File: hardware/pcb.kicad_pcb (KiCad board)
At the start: 2 copper layers, 80 x 30 mm, 4 parts

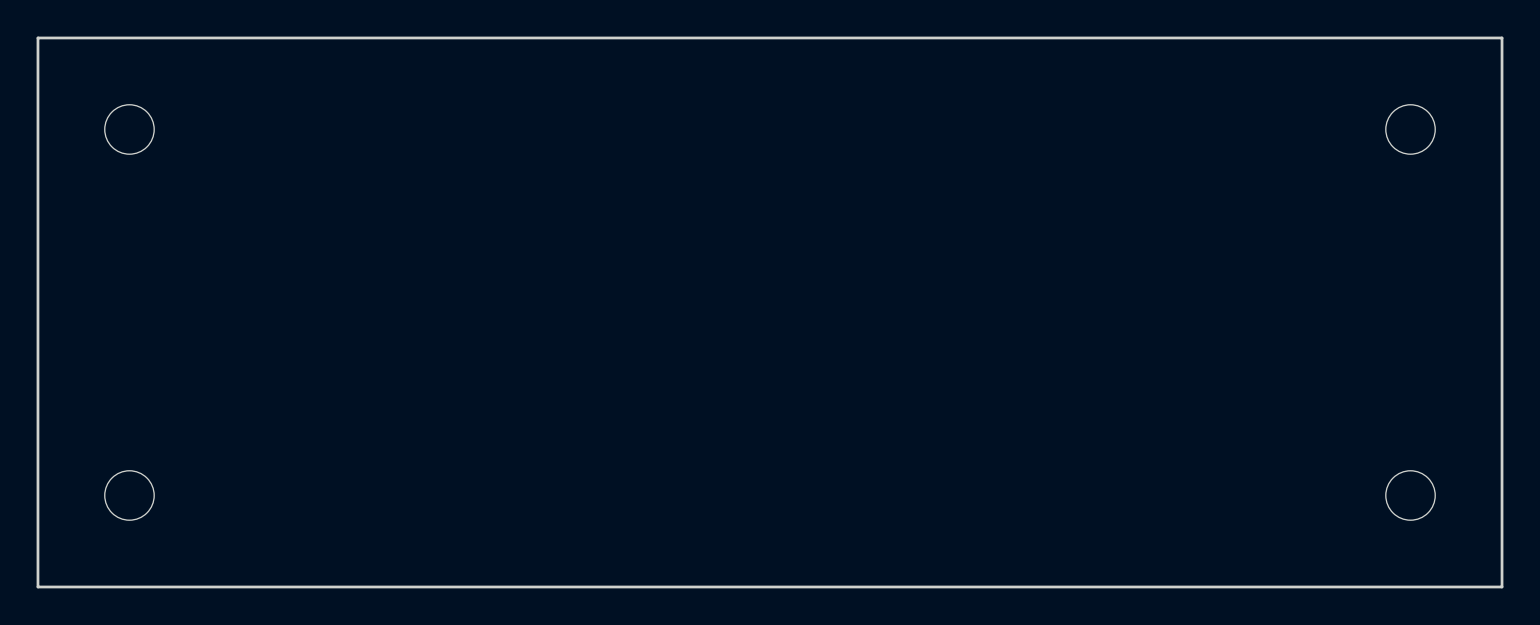
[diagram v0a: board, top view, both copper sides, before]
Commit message: Update PCB layout to show JST connectors on both sides
- Add component placement areas for balanced layout
- 2x JST connectors on left side (J3, J4 for D0, D1)
- 2x JST connectors on right side (J5, J6 for D2, D3)
- ESP32-C3 in center with CAN transceiver
- RJ45 on right, programming header bottom right
- Matches prototype photo layout
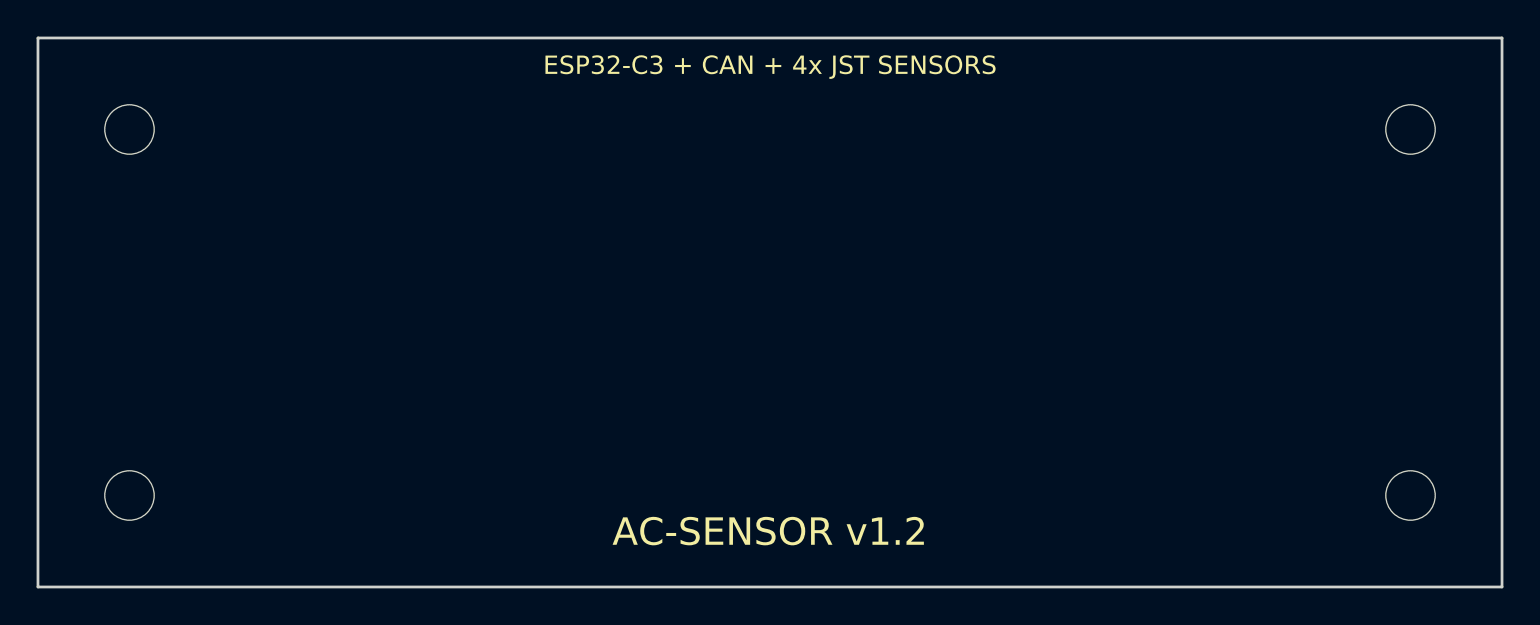
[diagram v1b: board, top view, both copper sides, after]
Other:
- board text added: "AC-SENSOR v1.2"
- board text added: "CAN: GPIO6(TX), GPIO7(RX) RJ45: 1(+5V), 2(GND), 3(H), 4(L)"
- board text added: "ESP32-C3 + CAN + 4x JST SENSORS"
- board text added: "ESP32-C3 CENTER"
- board text added: "J3 SENSOR 1 D0"
- board text added: "J4 SENSOR 2 D1"
- board text added: "J5 SENSOR 3 D2"
- board text added: "J6 SENSOR 4 D3"
- board text added: "JST LAYOUT: LEFT: J3(D0), J4(D1) RIGHT: J5(D2), J6(D3)"
- board text added: "POWER AMS1117-5.0"
- board text added: "PROG 4-PIN"
- board text added: "RJ45 CAN"
- board text added: "RST BOOT"
- board text added: "TJA1050"
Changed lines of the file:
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@@
     (paper "A4")
     (title_block
-      (title "ESP32-C3 CAN Bus + I2C Sensor Board")
+      (title "ESP32-C3 CAN Bus + 4x JST Sensor Board")
       (date "2025-06-02")
-      (rev "v1.0")
+      (rev "v1.2")
       (company "AC-Sensor Project")
-      (comment 1 "80mm x 30mm compact form factor")
+      (comment 1 "80mm x 30mm with JST connectors on both sides")
       (comment 2 "Optimized for JLCPCB automated assembly")
     )
@@
     )
     (pad_to_mask_clearance 0)
-    (pcbplotparams
-      (layerselection 0x00010fc_ffffffff)
-      (plot_on_all_layers_selection 0x0000000_00000000)
-      (disableapertmacros false)
-      (usegerberextensions false)
-      (usegerberattributes true)
-      (usegerberadvancedattributes true)
-      (creategerberjobfile true)
-      (dashed_line_dash_ratio 12.000000)
-      (dashed_line_gap_ratio 3.000000)
-      (svgprecision 4)
-      (plotframeref false)
-      (viasonmask false)
-      (mode 1)
-      (useauxorigin false)
-      (hpglpennumber 1)
-      (hpglpenspeed 20)
-      (hpglpendiameter 15.000000)
-      (dxfpolygonmode true)
-      (dxfimperialunits true)
-      (dxfusepcbnewfont true)
-      (psnegative false)
-      (psa4output false)
-      (plotreference true)
-      (plotvalue true)
-      (plotinvisibletext false)
-      (sketchpadsonfab false)
-      (subtractmaskfromsilk false)
-      (outputformat 1)
-      (mirror false)
-      (drillshape 1)
-      (scaleselection 1)
-      (outputdirectory "")
-    )
   )
   (net 0 "")
-  (net 1 "+3V3")
-  (net 2 "+5V")
-  (net 3 "GND")
-  (net 4 "CAN_TX")
-  (net 5 "CAN_RX")
-  (net 6 "CAN_H")
-  (net 7 "CAN_L")
-  (net 8 "I2C_SDA")
-  (net 9 "I2C_SCL")
-  (net 10 "CAN_SILENT")
-  (net 11 "STATUS_LED")
-  (net 12 "BOOT")
-  (net 13 "RESET")
-  (net 14 "UART_TX")
-  (net 15 "UART_RX")
+  (net 1 "+5V")
+  (net 2 "GND")
+  (net 3 "+3V3")
+  (net 4 "D0")
+  (net 5 "D1")
+  (net 6 "D2")
+  (net 7 "D3")
+  (net 8 "CAN_TX")
+  (net 9 "CAN_RX_FILTERED")
+  (net 10 "CAN_RX_RAW")
+  (net 11 "CAN_H")
+  (net 12 "CAN_L")
+  (net 13 "VIN")
+  (net 14 "RESET")
+  (net 15 "BOOT")
+  (net 16 "UART_TX")
+  (net 17 "UART_RX")
   ; Board outline - 80mm x 30mm
   (gr_rect (start 0 0) (end 80 30) (layer "Edge.Cuts") (width 0.15) (tstamp edge-cuts-1))
@@
   )
   ; Component placement areas (for layout reference)
-  ; ESP32-C3 module area
-  (gr_rect (start 15 10) (end 35 20) (layer "Cmts.User") (width 0.1) (tstamp esp32-area))
-  ; CAN transceiver area
-  (gr_rect (start 40 12) (end 50 18) (layer "Cmts.User") (width 0.1) (tstamp can-area))
-  ; RJ45 connector area
+  ; ESP32-C3 module area (center)
+  (gr_rect (start 30 10) (end 50 20) (layer "Cmts.User") (width 0.1) (tstamp esp32-area))
+  (gr_text "ESP32-C3\nCENTER" (at 40 15) (layer "Cmts.User")
+    (effects (font (size 1.5 1.5) (thickness 0.3)))
+  )
+  ; CAN transceiver area (right of ESP32)
+  (gr_rect (start 52 12) (end 62 18) (layer "Cmts.User") (width 0.1) (tstamp can-area))
+  (gr_text "TJA1050" (at 57 15) (layer "Cmts.User")
+    (effects (font (size 1.2 1.2) (thickness 0.25)))
+  )
+  ; RJ45 connector area (far right)
   (gr_rect (start 65 8) (end 78 22) (layer "Cmts.User") (width 0.1) (tstamp rj45-area))
-  ; Power regulation area
-  (gr_rect (start 15 22) (end 35 28) (layer "Cmts.User") (width 0.1) (tstamp power-area))
+  (gr_text "RJ45\nCAN" (at 71.5 15) (layer "Cmts.User")
+    (effects (font (size 1.2 1.2) (thickness 0.25)))
+  )
+  ; Power regulation area (top center)
+  (gr_rect (start 30 2) (end 50 8) (layer "Cmts.User") (width 0.1) (tstamp power-area))
+  (gr_text "POWER\nAMS1117-5.0" (at 40 5) (layer "Cmts.User")
+    (effects (font (size 1.0 1.0) (thickness 0.2)))
+  )
+  ; JST connectors on LEFT SIDE (2 connectors)
+  (gr_rect (start 2 8) (end 12 14) (layer "Cmts.User") (width 0.1) (tstamp jst-left-1))
+  (gr_text "J3\nSENSOR 1\nD0" (at 7 11) (layer "Cmts.User")
+    (effects (font (size 0.8 0.8) (thickness 0.15)))
+  )
+  (gr_rect (start 2 16) (end 12 22) (layer "Cmts.User") (width 0.1) (tstamp jst-left-2))
+  (gr_text "J4\nSENSOR 2\nD1" (at 7 19) (layer "Cmts.User")
+    (effects (font (size 0.8 0.8) (thickness 0.15)))
+  )
+  ; JST connectors on RIGHT SIDE (2 connectors)
+  (gr_rect (start 68 8) (end 78 14) (layer "Cmts.User") (width 0.1) (tstamp jst-right-1))
+  (gr_text "J5\nSENSOR 3\nD2" (at 73 11) (layer "Cmts.User")
+    (effects (font (size 0.8 0.8) (thickness 0.15)))
+  )
+  (gr_rect (start 68 16) (end 78 22) (layer "Cmts.User") (width 0.1) (tstamp jst-right-2))
+  (gr_text "J6\nSENSOR 4\nD3" (at 73 19) (layer "Cmts.User")
+    (effects (font (size 0.8 0.8) (thickness 0.15)))
+  )
+  ; Programming header area (bottom right)
+  (gr_rect (start 65 24) (end 78 28) (layer "Cmts.User") (width 0.1) (tstamp prog-area))
+  (gr_text "PROG\n4-PIN" (at 71.5 26) (layer "Cmts.User")
+    (effects (font (size 0.9 0.9) (thickness 0.18)))
+  )
+  ; Control buttons area (bottom left)
+  (gr_rect (start 2 24) (end 15 28) (layer "Cmts.User") (width 0.1) (tstamp buttons-area))
+  (gr_text "RST  BOOT" (at 8.5 26) (layer "Cmts.User")
+    (effects (font (size 0.9 0.9) (thickness 0.18)))
+  )
+  ; Board layout annotations
+  (gr_text "AC-SENSOR v1.2" (at 40 27) (layer "F.SilkS")
+    (effects (font (size 1.5 1.5) (thickness 0.3)))
+  )
+  (gr_text "ESP32-C3 + CAN + 4x JST SENSORS" (at 40 1.5) (layer "F.SilkS")
+    (effects (font (size 1.0 1.0) (thickness 0.2)))
+  )
+  ; Design notes
+  (gr_text "JST LAYOUT:\nLEFT: J3(D0), J4(D1)\nRIGHT: J5(D2), J6(D3)" (at 15 2) (layer "Cmts.User")
+    (effects (font (size 0.7 0.7) (thickness 0.14)))
+  )
+  (gr_text "CAN: GPIO6(TX), GPIO7(RX)\nRJ45: 1(+5V), 2(GND), 3(H), 4(L)" (at 55 2) (layer "Cmts.User")
+    (effects (font (size 0.7 0.7) (thickness 0.14)))
+  )
 )
